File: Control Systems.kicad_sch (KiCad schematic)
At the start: 34 parts, among them IC1 LM66200DRLR, J1 XT60-M, J2 47346-0001, J3 61300311121, J4 61300311121, J5 61300311121, J6 61300311121, J7 Conn_01x04_Pin, J8 SD_Card_Receptacle, U1 STM32F446RETx, U2 ICM-20948, U3 BMI088, U4 NEO-M8N-0, U5 MMC5983MA, U6 TL1963A-33DCYR, Y1 SIT8924BA-20.0

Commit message: Feat: Minor changes and fixes
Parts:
- removed IC1: LM66200DRLR, LM66200DRLR:SOT8, symbol LM66200DRLR:LM66200DRLR
- removed J7: Conn_01x04_Pin, symbol Connector:Conn_01x04_Pin
- removed J8: SD_Card_Receptacle, symbol Connector:SD_Card_Receptacle
- removed U2: ICM-20948, Sensor_Motion:InvenSense_QFN-24_3x3mm_P0.4mm, symbol Sensor_Motion:ICM-20948
- added C15, C16, C21: 100n, symbol Device:C
- added C17: 10uf, symbol Device:C
- added C18: 100nf, symbol Device:C
- added C19: 10nf, symbol Device:C
- added C20: 10u, symbol Device:C
- added C22, C23: 2u2, symbol Device:C
- added C24, C34, C35: 100n, symbol Device:C_Small
- added C25: 2.2n, symbol Device:C_Small
- added C26: 15p, symbol Device:C_Small
- added C27: 4.7u, symbol Device:C_Small
- added C28, C33: 1u, symbol Device:C_Small
- added C29, C32: 22u, symbol Device:C_Small
- added C30: 270u, symbol Device:C_Polarized_Small_US
- added C31: 180u, symbol Device:C_Polarized_Small_US
- added C36: 310n, symbol Device:C_Small
- added D1, D2, D20, D3, D4, D5, D6: ESD9B3.3ST5G, Diode_SMD:D_SOD-923, symbol Diode:ESD9B3.3ST5G
- added D10, D11, D15, D19, D8, D9: TVS, Diode_SMD:Nexperia_DSN1608-2_1.6x0.8mm, symbol Diode:PTVS10VZ1USK
- added D12, D13, D14, D7: SMAJ6.0CA, Diode_SMD:D_SMA, symbol Diode:SMAJ6.0CA
- added D16: RED, symbol Device:LED
- added D17, D18: Green, symbol Device:LED
- added FB1: 120R, symbol Device:FerriteBead
- added J10: Battery input, symbol Connector:Screw_Terminal_01x02
- added J11: Canbus, symbol Connector:Screw_Terminal_01x03
- added J12: Conn_02x03_Odd_Even, symbol Connector_Generic:Conn_02x03_Odd_Even
- added J14, J15: Conn_01x08_Socket, symbol Connector:Conn_01x08_Socket
- added J7: GPIO, symbol Connector:Screw_Terminal_01x03
- added J8: MEM2061-01-188-00-A_REVA, MEM2061-01-188-00-A_REVA:GCT_MEM2061-01-188-00-A_REVA, symbol MEM2061-01-188-00-A_REVA:MEM2061-01-188-00-A_REVA
- added J9: 5-1814832-2, 5-1814832-2:TE_5-1814832-2, symbol 5-1814832-2:5-1814832-2
- added L1: 27nH, symbol Device:L
- added L2: 5.6u, symbol Device:L
- added Q1, Q2: CSD18504Q5A, Package_TO_SOT_SMD:TDSON-8-1, symbol Transistor_FET:CSD18504Q5A
- added R10, R11, R4, R7, R8, R9: 47k, symbol Device:R
- added R12: 56k, symbol Device:R
- added R13: 80k, symbol Device:R
- added R14: 50k, symbol Device:R_Small
- added R15: 30.1k, symbol Device:R_Small
- added R16: 133k, symbol Device:R_Small
- added R17, R20: 100k, symbol Device:R_Small
- added R18: 16k, symbol Device:R_Small
- added R19: 383k, symbol Device:R_Small
- added R21, R22: 4.7, symbol Device:R_Small
- added R23, R24: 102k, symbol Device:R_Small
- added R25, R26, R27: 1K, symbol Device:R_Small
- added R5: 4k7, symbol Device:R
- added R6: 10, symbol Device:R
- added U10: TPS2121RUXR, TPS2121RUXR:IC_TPS2121RUXR, symbol TPS2121RUXRr:TPS2121RUXR
- added U2: LSM6DSL, Package_LGA:LGA-14_3x2.5mm_P0.5mm_LayoutBorder3x4y, symbol Sensor_Motion:LSM6DSL
- added U7: TPS552882QWRPMRQ1, TPS552882QWRPMRQ1:CONV_TPS552882QWRPMRQ1, symbol TPS552882QWRPMRQ1:TPS552882QWRPMRQ1
- added U8: USBLC6-2SC6, Package_TO_SOT_SMD:SOT-23-6, symbol Power_Protection:USBLC6-2SC6
- added U9: TPS1H200AQDGNRQ1, TPS1H200AQDGNRQ1:SOP65P490X110-9N, symbol TPS1H200AQDGNRQ1:TPS1H200AQDGNRQ1
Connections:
- net ADC1_IN1 is gone; now on net GPIO_EXTI1: U1.15 (PA1)
- net ADC1_INO is gone; now on net GPIO_EXTI0: U1.14 (PA0)
- net ADC_IN2 is gone; now on net GPIO_EXTI2: U1.16 (PA2)
- net GPIO_9 is gone; now on net GNSS_GPIO: U1.42 (PA9)
- net IMU_MISO is gone; now on net SPI1_MISO: U3.10 (SDO2), U3.15 (SDO1)
- net IMU_MOSI is gone; now on net SPI1_MOSI: U3.9 (SDA/SDI)
- net IMU_SCK is gone; now on net SPI1_SCK: U3.8 (SCL/SCK)
- net MAG_I2C1_SCL is gone; now on net I2C1_SCL: U5.1 (SCL/SPI_SCK)
- net MAG_I2C1_SDA is gone; now on net I2C1_SDA: U5.16 (SDA/SPI_SDI)
- net SPI2_NSS is gone; now on net SPI2_CS_2: U1.56 (PB4)
- net +3.3V: now also A1.1 (VDD), U4.22 (V_BCKP), U4.23 (VCC), U6.3 (OUT), C15.1, C16.1, C17.1, C18.1, C20.1, C21.1, D16.2 (A), D20.2 (A2), J12.2 (Pin_2), J14.5 (Pin_5), J8.4 (VDD), R10.1, R11.1, R12.2, R4.1, R5.1, R7.1, R8.1, R9.1, U2.5 (VDDIO), U2.8 (VDD); no longer J3.2, J4.2, J5.2, J6.2, U1.1 (VBAT), U1.13 (VDDA), U1.19 (VDD), U1.32 (VDD), U1.48 (VDD), U1.64 (VDD)
- net CAN2_RX: now also J11.1 (Pin_1)
- net CAN2_TX: now also J11.2 (Pin_2)
- net GND: now also J3.3, J4.3, J5.3, J6.3, C20.2, D1.1 (A1), D10.2 (A), D11.2 (A), D12.2 (A2), D13.2 (A2), D14.2 (A2), D2.1 (A1), D20.1 (A1), D3.1 (A1), D4.1 (A1), D5.1 (A1), D6.1 (A1), D7.2 (A2), D8.2 (A), D9.2 (A), J12.4 (Pin_4), J12.6 (Pin_6), J8.10 (CD2), J8.11 (GND), J8.12 (GND__1), J8.6 (VSS), R26.2
- net I2C1_SCL: now also R5.2, U2.13 (SCL)
- net I2C1_SDA: now also R4.2, U2.14 (SDA)
- net MCU_NRST: now also J12.5 (Pin_5)
- net PWM_TIM3_CH1: now also D7.1 (A1)
- net PWM_TIM3_CH2: now also D12.1 (A1)
- net PWM_TIM3_CH3: now also D13.1 (A1)
- net PWM_TIM3_CH4: now also D14.1 (A1)
- net SPI1_MISO: now also J15.2 (Pin_2)
- net SPI1_MOSI: now also J15.3 (Pin_3)
- net SPI1_SCK: now also J15.4 (Pin_4)
- net SPI2_MISO: now also A1.6 (SDO), U4.20 (TXD/SPI_MISO)
- net SPI2_MOSI: now also A1.7 (SDI/SDA), U4.21 (RXD/SPI_MOSI)
- net SPI2_SCK: now also A1.8 (SCLK), U4.19 (SCL/SPI_CLK)
- net SYS_SWCLK: now also J12.3 (Pin_3)
- net SYS_SWDIO: now also J12.1 (Pin_1)
- net GPIO_EXTI2: now reaches U5.15 (INT)
- net at C1.1, C2.1, C3.1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: now also U1.1 (VBAT), U1.13 (VDDA), U1.19 (VDD), U1.32 (VDD), U1.48 (VDD), U1.64 (VDD)
- net at U4.10 (GND): now also U4.12 (GND__1), U4.13 (GND__2), U4.24 (GND__3)
- net RF_IN: now reaches U4.11 (RF_IN)
- net RF_IN: now also J9.1, L1.1
- net SPI2_CS_2: now reaches U4.18 (SDA/SPI_CS_N)
- net GNSS_GPIO: now reaches U4.4 (EXTINT)
- net at U4.9 (VCC_RF): now also R6.1
- net at C12.2: now also C11.2
- net at U6.1 (IN): now also U10.1 (OUT), U10.1_1 (OUT), U10.8 (OUT), U10.8_1 (OUT); no longer J1.P (POS)
- net at U6.2 (GND_2): now also U6.4 (GND_4), R25.2
- net at A1.3 (GND): now also C21.2
- net SPI2_CS: now reaches A1.4 (~{CSB})
- net SPI2_CS: now also U1.55 (PB3)
- net GPIO_EXTI1: now reaches U3.12 (INT3)
- net SPI1_CS: now reaches U3.14 (CSB1)
- net SPI1_CS: now also U1.24 (PC4)
- net GPIO_EXTI0: now reaches U3.16 (INT1)
- net SPI1_CS_3: now reaches U3.5 (CSB2)
- net SPI1_CS_3: now also U1.59 (PB7)
- net GPIO_1: now reaches U1.11 (PC3)
- net GPIO_1: now also J7.1 (Pin_1)
- net RADIO_RST: now reaches U1.2 (PC13)
- net RADIO_RST: now also J15.6 (Pin_6)
- net SPI1_CS_2: now reaches U1.25 (PC5)
- net SPI1_CS_2: now also J15.5 (Pin_5)
- net SDIO_CK: now reaches U1.28 (PB2)
- net SDIO_CK: now also D6.2 (A2), J8.5 (CLK), R11.2
- net RADIO_D4: now reaches U1.3 (PC14)
- net RADIO_D4: now also J14.4 (Pin_4)
- net GP_LED: now reaches U1.36 (PB15)
- net GP_LED: now also D17.1 (K), D17.2 (A), R26.1
- net SDIO_D0: now reaches U1.39 (PC8)
- net SDIO_D0: now also D1.2 (A2), J8.7 (DAT0)
- net RADIO_D0: now reaches U1.4 (PC15)
- net RADIO_D0: now also J14.6 (Pin_6)
- net SDIO_NCD: now reaches U1.41 (PA8)
- net RX_LED: now reaches U1.50 (PA15)
- net RX_LED: now also D18.1 (K), D18.2 (A), R27.1
- net SDIO_D2: now reaches U1.51 (PC10)
- net SDIO_D2: now also D3.2 (A2), J8.1 (DAT2), R8.2
- net SDIO_D3: now reaches U1.52 (PC11)
- net SDIO_D3: now also D4.2 (A2), J8.2 (CD/DAT3), R9.2
- net RADIO_D5: now reaches U1.53 (PC12)
- net RADIO_D5: now also J15.7 (Pin_7)
- net SDIO_CMD: now reaches U1.54 (PD2)
- net SDIO_CMD: now also D5.2 (A2), J8.3 (CMD), R10.2
- net GPIO_2: now reaches U1.57 (PB5)
- net GPIO_2: now also J7.2 (Pin_2)
- net Servo_HS_Sw: now reaches U1.8 (PC0)
- net Servo_HS_Sw: now also U9.1 (IN)
- net at J2.2 (D-): now also U8.3 (I/O2)
- net at J2.3 (D+): now also U8.1 (I/O1)
- net at J2.5 (GND): now also C22.2, C23.2, U8.5 (VBUS)
- net ADC_IN3 renamed GPIO_EXTI3
- net GPIO_EXTI3: now also U2.4 (INT1)
- net GPIO_14 renamed GPIO_3
- net GPIO_3: now also J7.3 (Pin_3)
- net GPIO_9C renamed SDIO_D1
- net SDIO_D1: now also D2.2 (A2), J8.8 (DAT1), R7.2
- net SPI1_NSS renamed CAN_INT
- net CAN_INT: now also J11.3 (Pin_3)
- net USB_OTG_DM renamed USB_D_N
- net USB_D_N: now also U8.4 (I/O2)
- net USB_OTG_DP renamed USB_D_P
- net USB_D_P: now also U8.6 (I/O1)
- net VBUS renamed +VBUS
- net +VBUS: now also C22.1, FB1.1, U8.2 (GND)
- new net: U2.6 (GND), U2.7 (GND)
- new net: C19.1, L1.2, R6.2
- new net: C34.2, L2.1, Q1.1 (S), Q1.2 (S), Q1.3 (S), Q2.5 (D), U7.23 (SW1)
- new net: Q1.4 (G), R21.1
- new net: Q2.4 (G), R22.1
- new net: R22.2, U7.1 (DR1L)
- new net: C27.1, R24.1, U7.19 (VCC), U7.5 (PG)
- new net: R23.2, R24.2
- new net: C35.1, L2.2, U7.21 (SW2), U7.25 (SW2__1)
- new net: C25.1, C26.1, U7.18 (COMP)
- new net: C26.2, R14.2, R16.2, U7.15 (MODE), U7.7 (DITH/SYNC)
- new net: R14.1, U7.8 (FSW)
- new net: Q2.1 (S), Q2.2 (S), Q2.3 (S), R15.1, U7.10 (AGND), U7.24 (PGND__1), U7.9 (PGND)
- new net: R15.2, U7.17 (ILIM)
- new net: R21.2, U7.2 (DR1H)
- new net: R23.1, U7.6 (~{CC})
- new net: C24.1, U10.11 (SS)
- new net: C28.2, C29.2, C30.2, R18.2
- new net: C25.2, R16.1
- new net: C31.2, C32.2, C33.2, R20.2
- new net: C17.2, C18.2
- new net: D19.1 (K), J10.2 (Pin_2), U10.7 (IN1), U10.7_1 (IN1)
- new net: D19.2 (A), J10.1 (Pin_1)
- new net: C36.2, U9.2 (DIAG_EN)
- new net: U9.4 (CL), U9.6 (GND)
- new net: C36.1, U9.5 (DELAY)
- new net: R13.1, U10.10 (ILIM)
- new net: U10.12 (GND), U10.9 (ST)
- new net: C23.1, FB1.2, U10.2 (IN2), U10.2_1 (IN2)
- new net: U10.3 (CP2), U10.4 (OV2), U10.5 (OV1), U10.6 (PR1)
- new net: J9.S1, J9.S2, J9.S3, J9.S4
- new net +8.2V: C28.1, C29.1, C30.1, R17.1, U7.11 (VOUT), U7.12 (ISP), U7.13 (ISN), U7.26 (VOUT__1), U9.8 (VS)
- new net PWR_LED_K: D16.1 (K), R25.1
- new net SD_NCD: J8.9 (CD1), R12.1
- new net SWR_BOOT1: C34.1, U7.22 (BOOT1)
- new net SWR_BOOT2: C35.2, U7.20 (BOOT2)
- new net SWR_EN: R19.2, R20.1, U7.4 (EN/UVLO)
- new net SWR_FB: R17.2, R18.1, U7.14 (FB)
- new net Servo +8.2V: D10.1 (K), D11.1 (K), D8.1 (K), D9.1 (K), J3.2, J4.2, J5.2, J6.2, U9.7 (OUT)
- new net VIN_7.4V: C31.1, C32.1, C33.1, D15.1 (K), J1.P (POS), Q1.5 (D), R19.1, U7.3 (VIN)
- no-connect marks 1 -> 23
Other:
- note added: "4.1.2 of DTEG IREC RULES: States that tracking elements (GPS) must be powered seperatly So added a second screw terminal for just PCB power can be 3.7-7.4V"
- note added: "433mHz LORA radio"
- note added: "High Side switch no current limiting"
- note added: "I DONT CARE ANYMORE IM JUST PROVIDING POWER FOR 2 SERVOS AHHHHHH FUCK THIS DUDE"
- note added: "REVIEW THIS VCC DIAGRAM"
- note added: "SD CARD receptacle"
- note added: "VERIFY PI FILTER AND TVS DIODE"
- note added: "Verify PINOUT for STM"
- note removed: "Figure out SWD wiring"
- note removed: "Finish Pi filter or other filter and TVS diode"
- note removed: "Switching diode for USB & battery power"
- moved on the sheet: A1, C1, C2, C3, C4, C5, C6, C7, C8, J1, J2, J3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

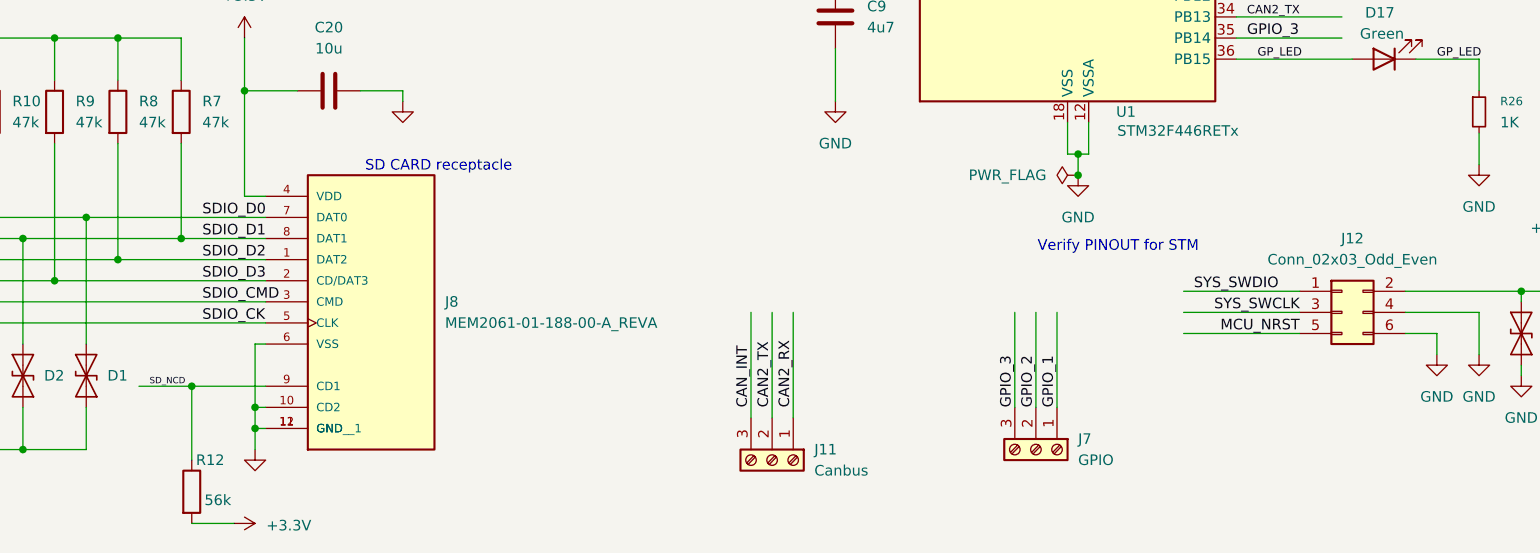
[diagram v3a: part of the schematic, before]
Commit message: Feat: added USB RX and TX headers
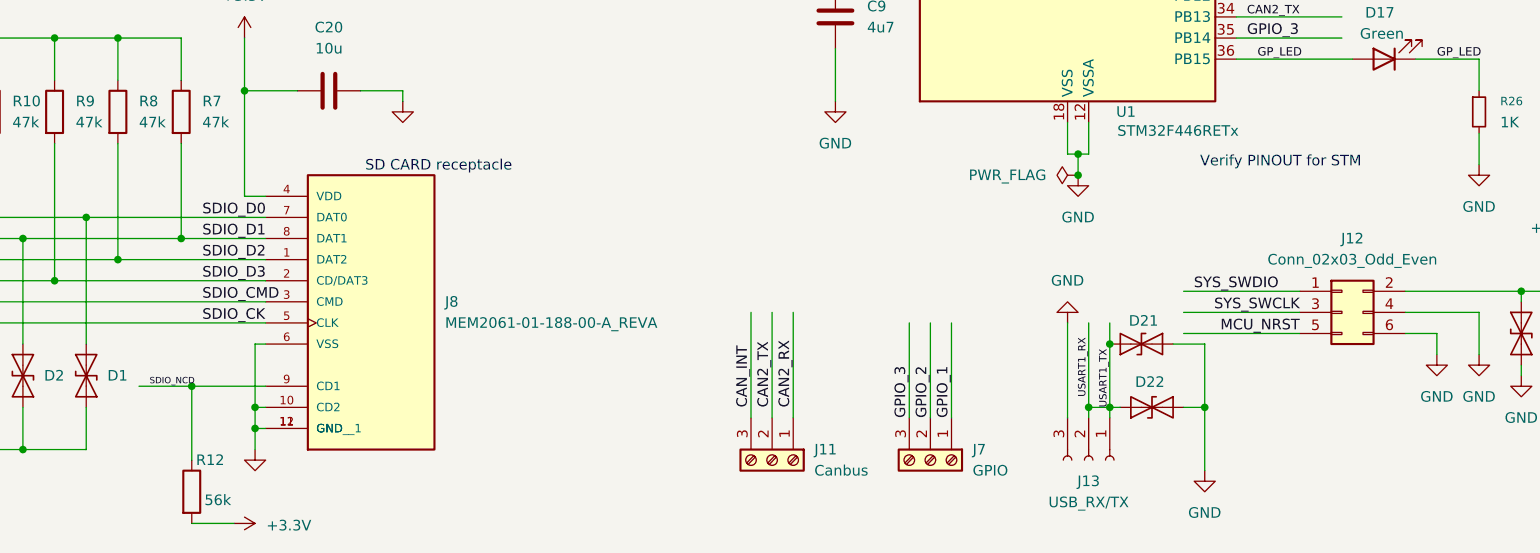
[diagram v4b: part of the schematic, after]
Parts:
- added D21, D22: ESD9B3.3ST5G, Diode_SMD:D_SOD-923, symbol Diode:ESD9B3.3ST5G
- added J13: USB_RX/TX, symbol Connector:Conn_01x03_Socket
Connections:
- net SD_NCD is gone; now on net SDIO_NCD: J8.9 (CD1), R12.1
- net USART1_TX is gone; now on net USART1_RX: U1.58 (PB6)
- net GND: now also D21.1 (A1), D22.1 (A1), J13.3 (Pin_3)
- net USART1_RX: now also D21.2 (A2), D22.2 (A2), J13.1 (Pin_1), J13.2 (Pin_2)
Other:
- moved on the sheet: J7

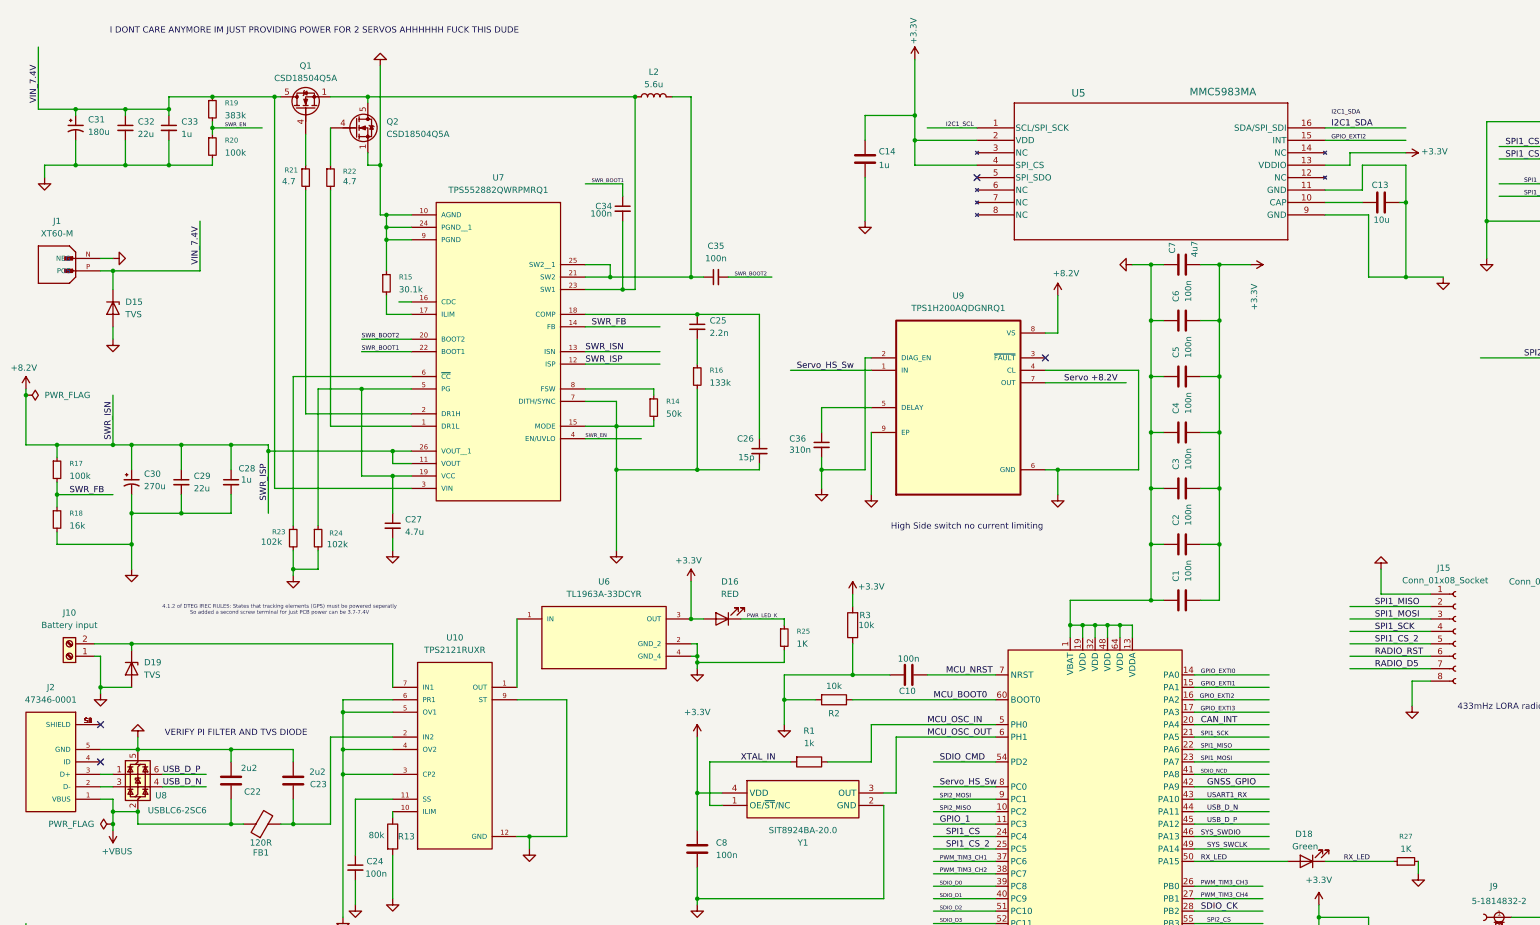
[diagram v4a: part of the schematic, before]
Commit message: Feat: Finished ERC, Starting routing
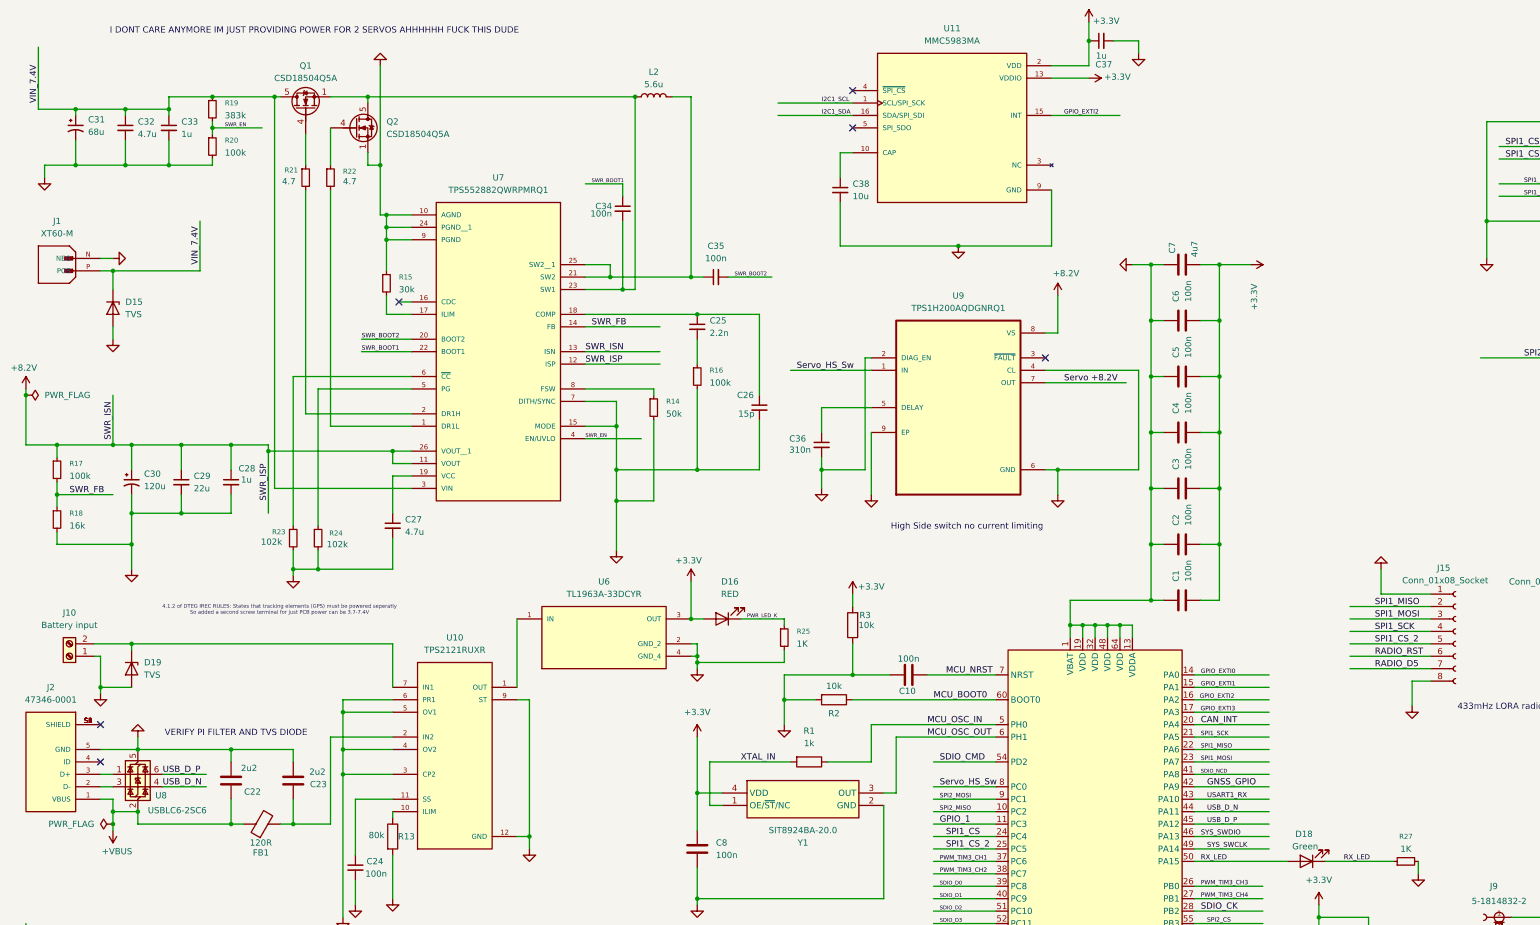
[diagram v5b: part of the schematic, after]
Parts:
- removed C13: 10u, symbol Device:C
- removed C14: 1u, symbol Device:C
- removed U5: MMC5983MA, MMC5983MA_MEM, symbol 2025-11-07_18-39-49:MMC5983MA
- added C37: 1u, symbol Device:C_Small
- added C38: 10u, symbol Device:C_Small
- added U11: MMC5983MA, MMC5983MA:PQFN50P300X300X100-16N, symbol MMC5983MA:MMC5983MA
- C30: value 270u -> 120u
- C31: value 180u -> 68u
- C32: value 22u -> 4.7u
- J1: Availability Not in stock -> In Stock
- R15: value 30.1k -> 30k
- R16: value 133k -> 100k
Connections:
- net +3.3V: now also C37.1, U11.13 (VDDIO), U11.2 (VDD)
- net GND: now also C38.2, U11.11 (GND), U11.9 (GND)
- net GPIO_EXTI2: now also U11.15 (INT)
- net I2C1_SCL: now also U11.1 (SCL/SPI_SCK)
- net I2C1_SDA: now also U11.16 (SDA/SPI_SDI)
- net at C27.1, U7.19 (VCC): no longer R24.1, U7.5 (PG)
- net at C27.2: now also R23.2, R24.2
- new net: C38.1, U11.10 (CAP)
- new net: U11.12 (NC), U11.14 (NC), U11.3 (NC), U11.6 (NC), U11.7 (NC), U11.8 (NC)
- new net: R24.1, U7.5 (PG)
- no-connect marks 23 -> 25
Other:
- moved on the sheet: C26

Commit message: Feat: PCB footprints and models assigned, basic routing finished
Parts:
- removed J2: 47346-0001, 47346-0001:MOLEX_47346-0001, symbol 47346-0001:47346-0001
- removed J3, J4, J5, J6: 61300311121, 61300311121:WURTH_61300311121, symbol 61300311121:61300311121
- removed J7: GPIO, symbol Connector:Screw_Terminal_01x03
- removed U4: NEO-M8N-0, NEO-M8N-0:XCVR_NEO-M8N-0, symbol NEO-M8N-0:NEO-M8N-0
- added J16, J3, J4, J5: Conn_01x03_Pin, Connector_PinHeader_2.54mm:PinHeader_1x03_P2.54mm_Vertical, symbol Connector:Conn_01x03_Pin
- added J2: 10118194-0001LF, imports:AMPHENOL_10118194-0001LF, symbol 10118194-0001LF:10118194-0001LF
- added J7: USB_RX/TX, Connector_PinSocket_2.54mm:PinSocket_1x03_P2.54mm_Vertical, symbol Connector:Conn_01x03_Socket
- added U5: NEO-M8N-0, imports:XCVR_NEO-M8N-0, symbol NEO-M8N-0:NEO-M8N-0
- A1: footprint MS561101BA03-50:XDCR_MS561101BA03-50 -> imports:XDCR_MS561101BA03-50
- C1, C10, C11, C12, C15, C16, C2, C21, C22, C23, C24, C25, C26, C27, C28, C3, C32, C33, C34, C35, C36, C37, C4, C5, C6, C7, C8, C9: footprint (none) -> Capacitor_SMD:C_0402_1005Metric
- C17: value 10uf -> 10u; footprint (none) -> Capacitor_SMD:C_0603_1608Metric
- C18: value 100nf -> 100n; footprint (none) -> Capacitor_SMD:C_0402_1005Metric
- C19: value 10nf -> 10n; footprint (none) -> Capacitor_SMD:C_0402_1005Metric
- C20, C38: footprint (none) -> Capacitor_SMD:C_0603_1608Metric
- C29, C30, C31: footprint (none) -> Capacitor_SMD:C_0805_2012Metric
- D16, D17, D18: footprint (none) -> LED_SMD:LED_0603_1608Metric
- FB1, L1, L2: footprint (none) -> Inductor_SMD:L_0603_1608Metric
- J1: footprint XT60-M:AMASS_XT60-M -> imports:AMASS_XT60-M
- J10: footprint (none) -> Connector_Wago:Wago_734-162_1x02_P3.50mm_Horizontal
- J11: footprint (none) -> Connector_Wago:Wago_734-163_1x03_P3.50mm_Horizontal
- J12: footprint (none) -> Connector_PinHeader_2.54mm:PinHeader_2x03_P2.54mm_Vertical
- J13: footprint (none) -> Connector_PinSocket_2.54mm:PinSocket_1x03_P2.54mm_Vertical
- J14, J15: footprint (none) -> Connector_PinSocket_2.54mm:PinSocket_1x08_P2.54mm_Vertical
- J8: footprint MEM2061-01-188-00-A_REVA:GCT_MEM2061-01-188-00-A_REVA -> imports:GCT_MEM2061-01-188-00-A_REVA
- J9: footprint 5-1814832-2:TE_5-1814832-2 -> imports:SMA_CONN_TE_5-1814832-2
- R1, R2, R21, R22, R25, R26, R27, R3, R5, R6: footprint (none) -> Resistor_SMD:R_0402_1005Metric
- R10, R11, R12, R13, R14, R15, R16, R17, R18, R19, R20, R23, R24, R4, R7, R8, R9: footprint (none) -> Resistor_SMD:R_0603_1608Metric
- U10: footprint TPS2121RUXR:IC_TPS2121RUXR -> imports:IC_TPS2121RUXR
- U11: footprint MMC5983MA:PQFN50P300X300X100-16N -> MMC5983MA(1):PQFN50P300X300X100-16N
- U3: footprint BMI088:PQFN50P450X300X100-16N -> imports:BMI088
- U6: footprint TL1963A-33DCYR:VREG_TL1963A-33DCYR -> imports:VREG_TL1963A-33DCYR
- U7: footprint TPS552882QWRPMRQ1:CONV_TPS552882QWRPMRQ1 -> imports:CONV_TPS552882QWRPMRQ1
- U9: footprint TPS1H200AQDGNRQ1:SOP65P490X110-9N -> imports:TPS1H200
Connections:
- net +3.3V: now also U1.1 (VBAT), U1.13 (VDDA), U1.19 (VDD), U1.32 (VDD), U1.48 (VDD), U1.64 (VDD), U5.22 (V_BCKP), U5.23 (VCC)
- net +VBUS: now also J2.1 (VCC)
- net GND: now also J16.1 (Pin_1), J3.1 (Pin_1), J4.1 (Pin_1), J5.1 (Pin_1)
- net GNSS_GPIO: now also U5.4 (EXTINT)
- net GPIO_1: now also J7.1 (Pin_1)
- net GPIO_2: now also J7.2 (Pin_2)
- net GPIO_3: now also J7.3 (Pin_3)
- net PWM_TIM3_CH1: now also J16.3 (Pin_3)
- net PWM_TIM3_CH2: now also J3.3 (Pin_3)
- net PWM_TIM3_CH3: now also J4.3 (Pin_3)
- net PWM_TIM3_CH4: now also J5.3 (Pin_3)
- net RF_IN: now also U5.11 (RF_IN)
- net SPI2_CS_2: now also U5.18 (SDA/SPI_CS_N)
- net SPI2_MISO: now also U5.20 (TXD/SPI_MISO)
- net SPI2_MOSI: now also U5.21 (RXD/SPI_MOSI)
- net SPI2_SCK: now also U5.19 (SCL/SPI_CLK)
- net Servo +8.2V: now also J16.2 (Pin_2), J3.2 (Pin_2), J4.2 (Pin_2), J5.2 (Pin_2)
- net at C1.1, C2.1, C3.1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: no longer U1.1 (VBAT), U1.13 (VDDA), U1.19 (VDD), U1.32 (VDD), U1.48 (VDD), U1.64 (VDD)
- net at R6.1: now also U5.9 (VCC_RF)
- net at C22.2, C23.2, U8.5 (VBUS): now also J2.5 (GND)
- net +VBUSF: now reaches C23.1, FB1.2, U10.2 (IN2), U10.2_1 (IN2)
- net at U8.3 (I/O2): now also J2.2 (D-)
- net at U8.1 (I/O1): now also J2.3 (D+)
- new net: J2.SH1 (SHIELD), J2.SH2 (SHIELD), J2.SH3 (SHIELD), J2.SH4 (SHIELD), J2.SH5 (SHIELD), J2.SH6 (SHIELD)
- new net: U5.10 (GND), U5.12 (GND__1), U5.13 (GND__2), U5.24 (GND__3)
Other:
- moved on the sheet: C22, C23, FB1, U8
